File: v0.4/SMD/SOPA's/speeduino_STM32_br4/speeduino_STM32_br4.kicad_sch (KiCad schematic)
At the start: 1 part, among them U1 STM32F405RGT6

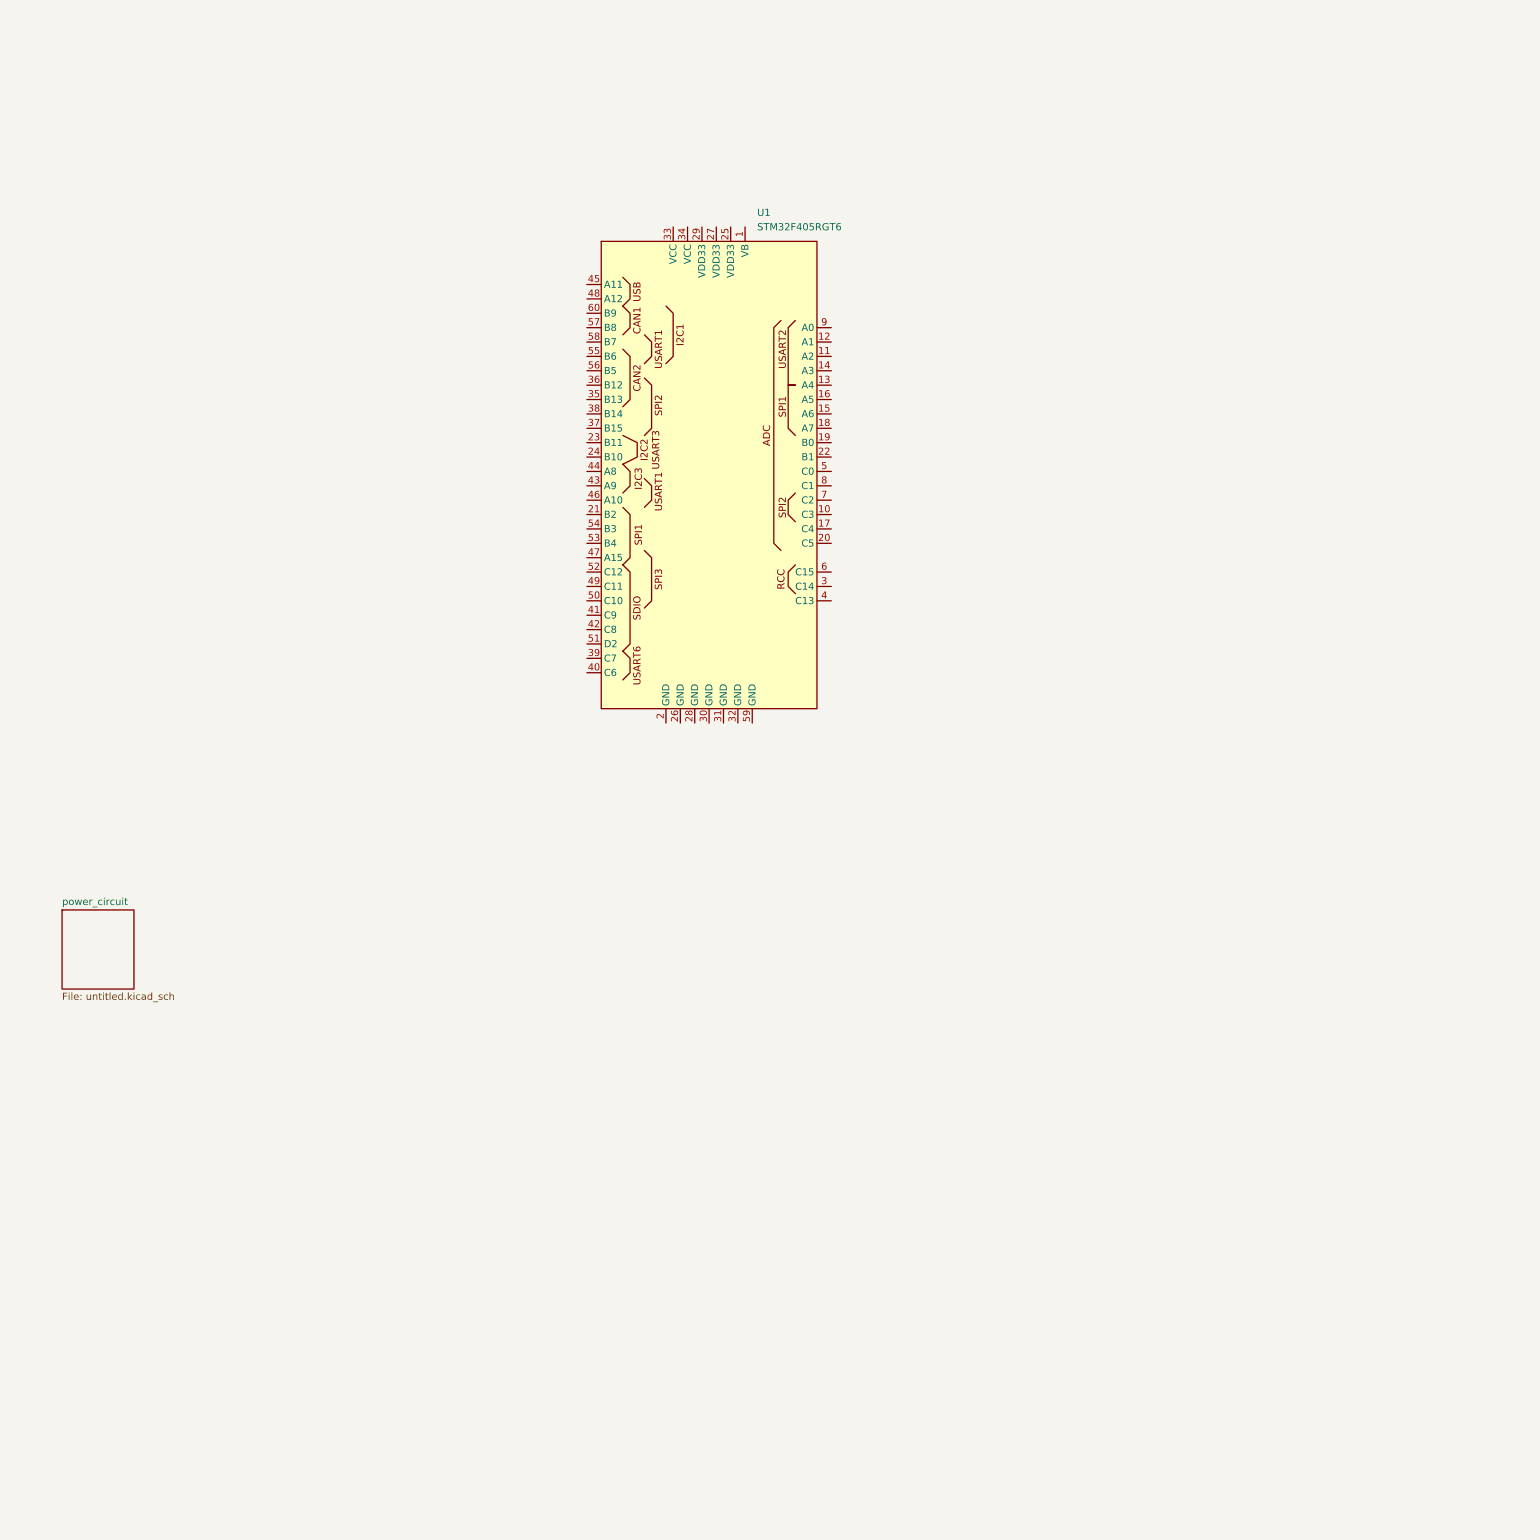
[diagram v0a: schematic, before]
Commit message: Add CAN communication schematic and related files
Added new KiCad schematic for CAN communication, associated backup files, and related PDFs to the v0.4/SMD/SOPA's/speeduino_STM32_br4 directory. Also included slla271.pdf and updated project and schematic files to reflect these additions.
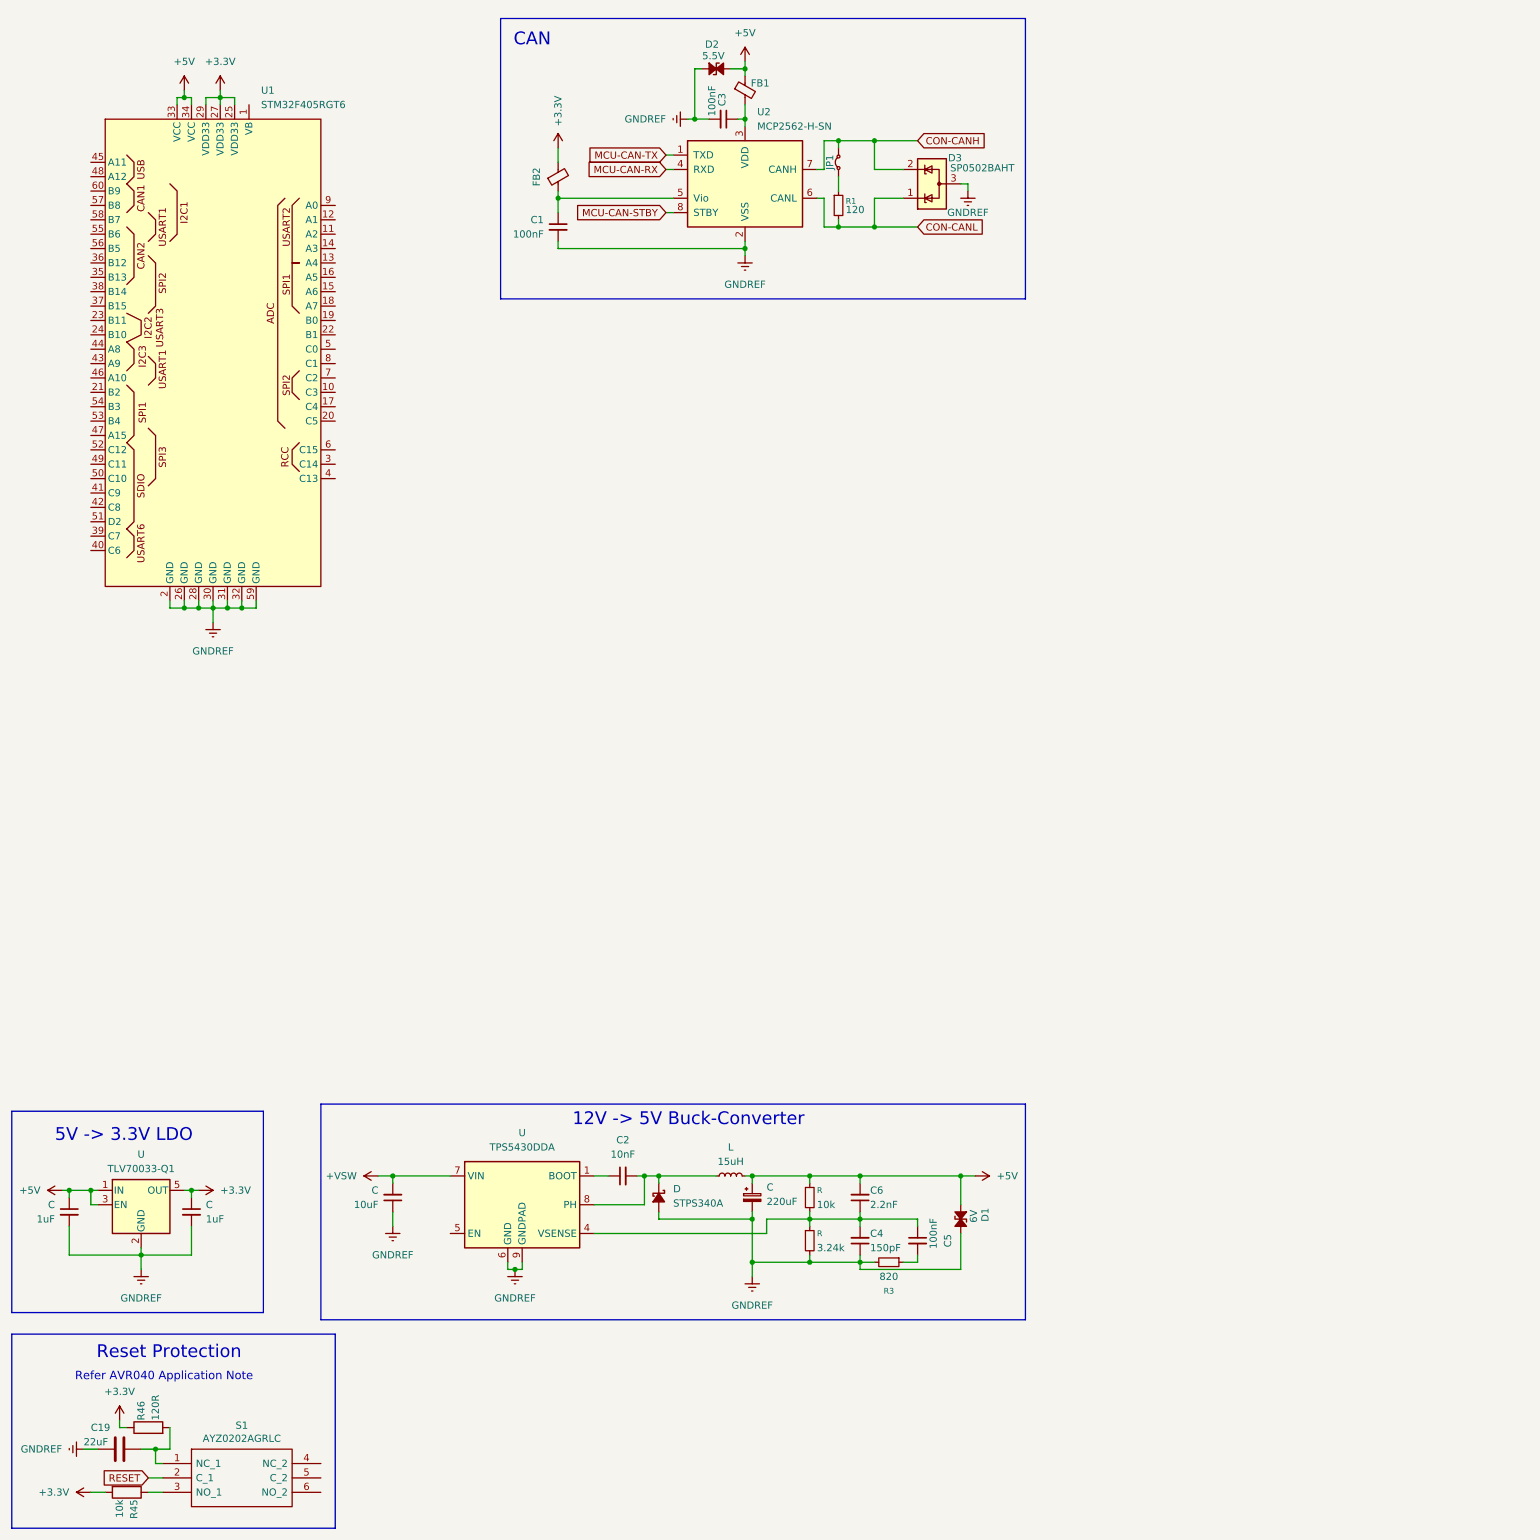
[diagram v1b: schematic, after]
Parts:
- added C (x2): 1uF, symbol Device:C_Small
- added C: 10uF, Capacitor_SMD:C_0603_1608Metric_Pad1.08x0.95mm_HandSolder, symbol Device:C_Small
- added C: 220uF, Capacitor_SMD:C_Elec_4x5.8, symbol Device:C_Polarized_Small
- added C1, C3: 100nF, symbol Device:C_Small
- added C19: 22uF, Capacitor_SMD:C_0805_2012Metric_Pad1.15x1.40mm_HandSolder, symbol Device:C
- added C2: 10nF, Capacitor_SMD:C_0603_1608Metric_Pad1.08x0.95mm_HandSolder, symbol Device:C_Small
- added C4: 150pF, Capacitor_SMD:C_0603_1608Metric_Pad1.08x0.95mm_HandSolder, symbol Device:C_Small
- added C5: 100nF, Capacitor_SMD:C_0603_1608Metric_Pad1.08x0.95mm_HandSolder, symbol Device:C_Small
- added C6: 2.2nF, Capacitor_SMD:C_0603_1608Metric_Pad1.08x0.95mm_HandSolder, symbol Device:C_Small
- added D: STPS340A, symbol Device:D_Schottky_Small_Filled
- added D1: 6V, Diode_SMD:D_0805_2012Metric, symbol Device:D_TVS_Small_Filled
- added D2: 5.5V, Diode_SMD:D_0805_2012Metric, symbol Device:D_TVS_Small_Filled
- added D3: SP0502BAHT, Package_TO_SOT_SMD:SOT-23, symbol Power_Protection:SP0502BAHT
- added FB1, FB2: FerriteBead_Small, symbol Device:FerriteBead_Small
- added JP1: J-Term, TestPoint:TestPoint_2Pads_Pitch2.54mm_Drill0.8mm, symbol Jumper:Jumper_2_Small_Bridged
- added L: 15uH, Inductor_SMD:L_12x12mm_H8mm, symbol Device:L_Small
- added R: 10k, symbol Device:R_Small
- added R: 3.24k, symbol Device:R_Small
- added R1: 120, symbol Device:R_Small
- added R3: 820, symbol Device:R_Small
- added R45: 10k, Resistor_SMD:R_0805_2012Metric, symbol Device:R
- added R46: 120R, Resistor_SMD:R_0805_2012Metric, symbol Device:R
- added S1: AYZ0202AGRLC, Misc:AYZ0202AGRLC, symbol v0.4.4c-rescue:AYZ0202AGRLC-Misc
- added U: TLV70033-Q1, Package_TO_SOT_SMD:SOT-23-5, symbol Regulator_Linear:TLV70033_SOT23-5
- added U: TPS5430DDA, Package_SO:TI_SO-PowerPAD-8_ThermalVias, symbol Regulator_Switching:TPS5430DDA
- added U2: MCP2562-H-SN, Package_SO:SOIC-8_3.9x4.9mm_P1.27mm, symbol Interface_CAN_LIN:MCP2562-H-SN
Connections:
- net GNDREF: now reaches U1.2 (GND)
- net GNDREF: now also U1.26 (GND), U1.28 (GND), U1.30 (GND), U1.31 (GND), U1.32 (GND), U1.59 (GND), C.1, C.2, C.2, C.2, C1.2, C19.2, C3.2, C4.1, D.2 (A), D1.2 (A2), D2.1 (A1), D3.3 (A), R.2, R3.2, U.2 (GND), U.6 (GND), U.9 (GNDPAD), U2.2 (VSS)
- net +3.3V: now reaches U1.25 (VDD33)
- net +3.3V: now also U1.27 (VDD33), U1.29 (VDD33), C.1, FB2.2, R45.2, R46.1, U.5 (OUT)
- net +5V: now reaches U1.33 (VCC)
- net +5V: now also U1.34 (VCC), C.1, C.1, C6.2, D1.1 (A1), D2.2 (A2), FB1.1, L.2, R.1, U.1 (IN), U.3 (EN)
- new net: C19.1, R46.2, S1.1 (NC_1)
- new net: R45.1, S1.3 (NO_1)
- new net: JP1.1 (A), R1.1
- new net: C4.2, C5.1, C6.1, R.1, R.2, U.4 (VSENSE)
- new net: C2.2, D.1 (K), L.1, U.8 (PH)
- new net: C3.1, FB1.2, U2.3 (VDD)
- new net: C1.1, FB2.1, U2.5 (Vio)
- new net: C2.1, U.1 (BOOT)
- new net: C5.2, R3.1
- new net +VSW: C.2, U.7 (VIN)
- new net CON-CANH: D3.2 (K), JP1.2 (B), U2.7 (CANH)
- new net CON-CANL: D3.1 (K), R1.2, U2.6 (CANL)
- new net MCU-CAN-RX: U2.4 (RXD)
- new net MCU-CAN-STBY: U2.8 (STBY)
- new net MCU-CAN-TX: U2.1 (TXD)
- new net RESET: S1.2 (C_1)
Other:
- removed sheet power_circuit
- note added: "12V -> 5V Buck-Converter"
- note added: "5V -> 3.3V LDO"
- note added: "CAN"
- note added: "Refer AVR040 Application Note"
- note added: "Reset Protection"
- company: (none) -> Luis Felipe Marcon Brunhara
- title: (none) -> Sopa's Speeduino32 Basic
- moved on the sheet: U1

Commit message: Added Fuel & Ignition
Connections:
- net MCU-CAN-RX: now also U1.57 (B8)
- net MCU-CAN-TX: now also U1.60 (B9)
- net GNDREF renamed GND
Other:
- added sheet Fuel (fuel.kicad_sch)
- added sheet Ignition (ignition.kicad_sch)
- moved on the sheet: C, C1, C19, C2, C3, C4, C5, C6, D, D1, D2, D3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
